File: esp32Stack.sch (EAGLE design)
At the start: 23 parts, among them J02 470, J04 470, J05 470, J12 470, J13 470

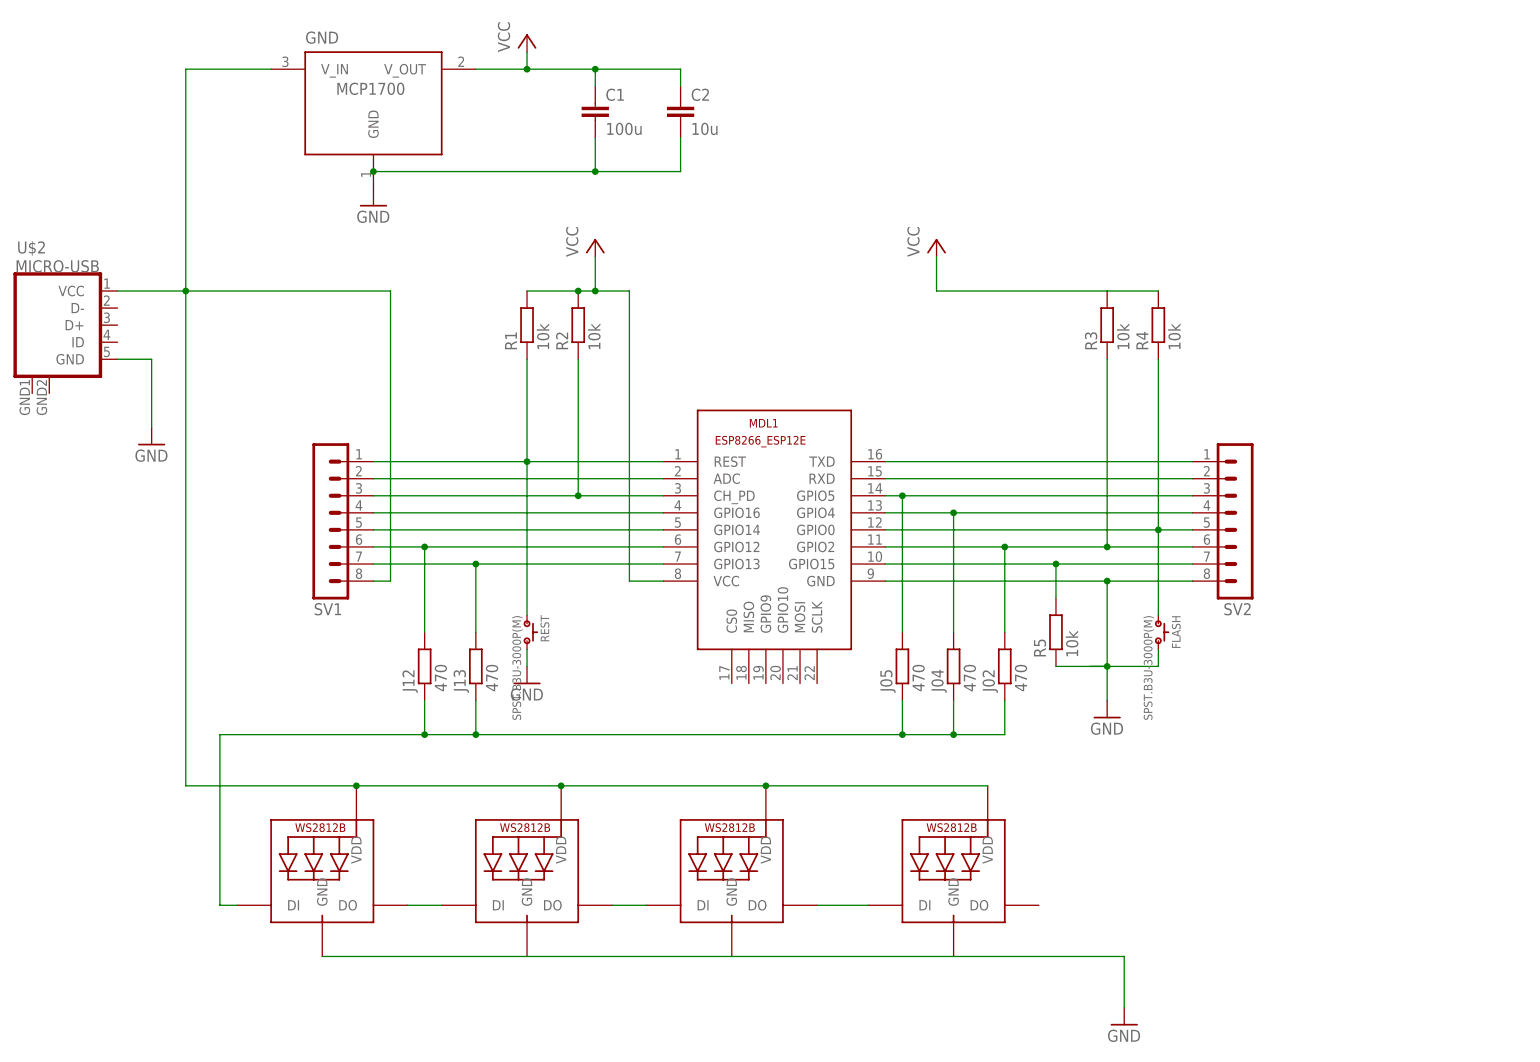
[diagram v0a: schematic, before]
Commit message: added an ftdi version
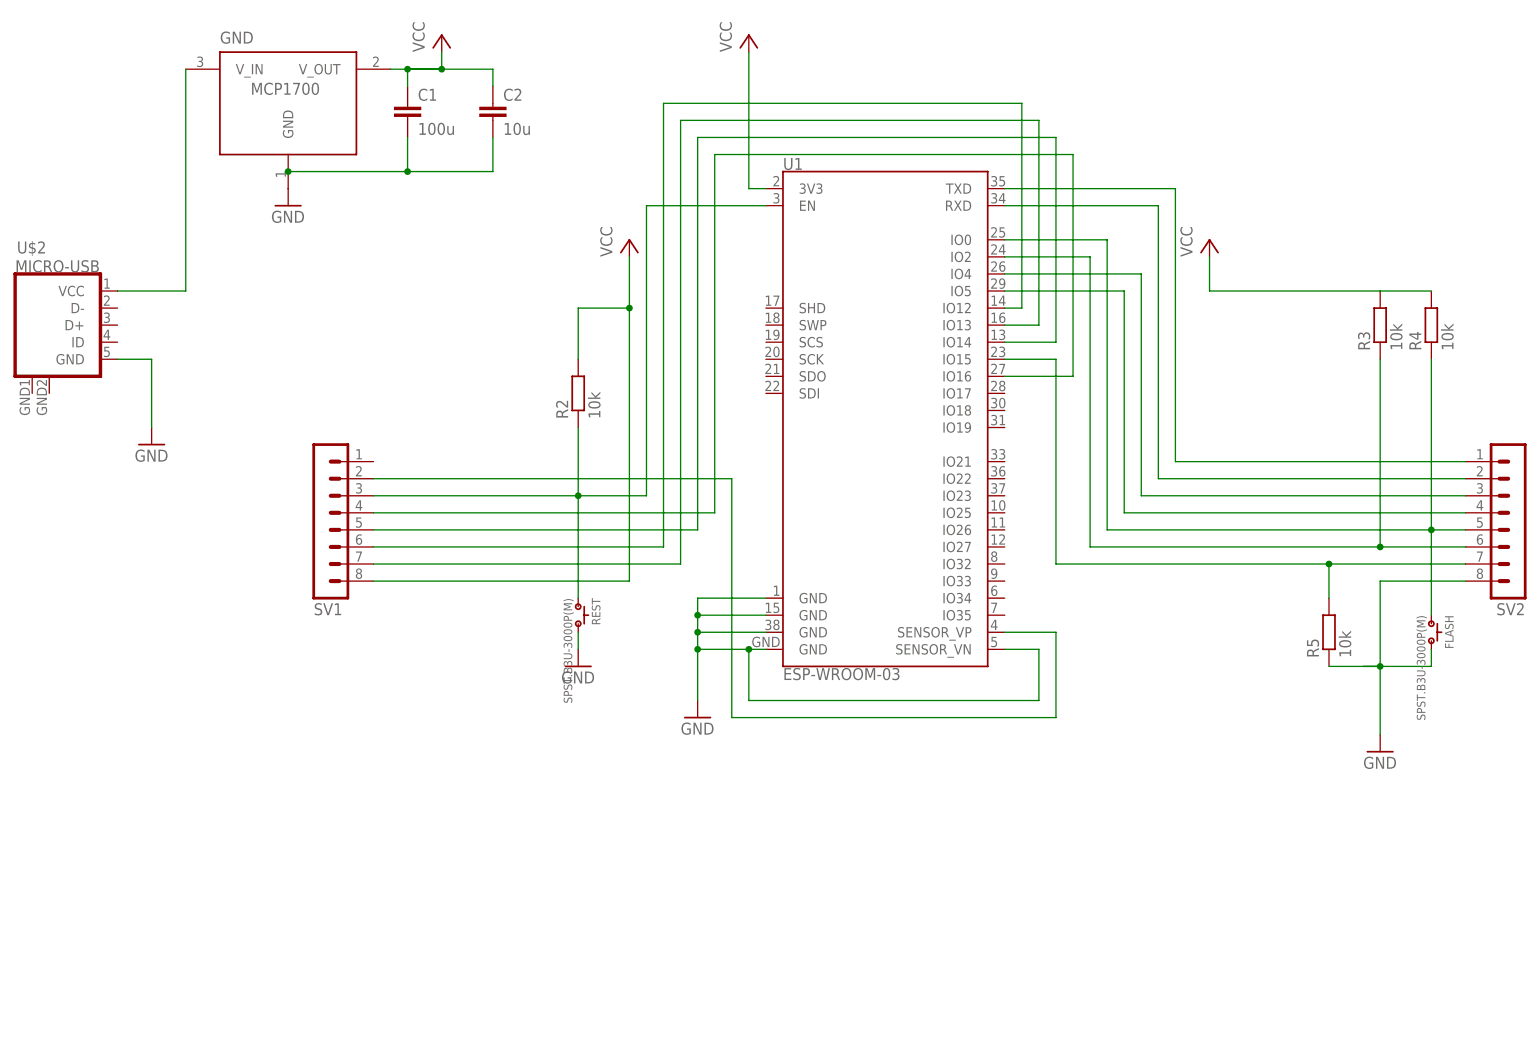
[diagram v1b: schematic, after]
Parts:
- removed J02, J04, J05, J12, J13: 470, eagle-ltspice:R
- removed LED1, LED2, LED3, LED4: WS2812B5050, adafruit:WS2812B5050
- removed MDL1: (no value), ESP12E:ESP8266-12EESP8266-ESP12E
- removed R1: 10k, eagle-ltspice:R
- added U1: ESP-WROOM-03, esp32:ESP-WROOM-03
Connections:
- removed net 3V3: C1.1, C2.1, GND.V_OUT, MDL1.VCC, R1.2, R2.2, R3.2, R4.2
- removed net 5V: GND.V_IN, LED1.VDD, LED2.VDD, LED3.VDD, LED4.VDD, SV1.8, U$2.VCC
- removed net CH_PD: MDL1.CH_PD, R2.1, SV1.3
- removed net DIN: J02.1, J04.1, J05.1, J12.1, J13.1, LED1.DI
- removed net DOUT1DIN2: LED1.DO, LED2.DI
- removed net DOUT2DIN3: LED2.DO, LED3.DI
- removed net DOUT3DIN4: LED3.DO, LED4.DI
- removed net GPIO16: MDL1.GPIO16, SV1.4
- removed net REST: MDL1.REST, R1.1, REST.1, SV1.1
- removed net RXD: MDL1.RXD, SV2.2
- removed net TXD: MDL1.TXD, SV2.1
- new net EN: R2.1, REST.1, SV1.3, U1.EN
- new net N$1: SV2.1, U1.TXD
- new net N$2: SV2.2, U1.RXD
- new net N$3: SV1.5, U1.IO14
- new net N$4: GND.V_IN, U$2.VCC
- new net VCC/V3.3: C1.1, C2.1, GND.V_OUT, R2.2, R3.2, R4.2, SV1.8, U1.3V3
- net ADC: now also U1.SENSOR_VP; no longer MDL1.ADC
- net GND: now also U1.GND, U1.GND@1, U1.GND@15, U1.GND@38, U1.SENSOR_VN; no longer LED1.GND, LED2.GND, LED3.GND, LED4.GND, MDL1.GND
- net GPIO0: now also U1.IO0; no longer MDL1.GPIO0
- net GPIO12: now also U1.IO12; no longer J12.2, MDL1.GPIO12
- net GPIO13: now also U1.IO13; no longer J13.2, MDL1.GPIO13
- net GPIO14: now also SV1.4, U1.IO16; no longer MDL1.GPIO14, SV1.5
- net GPIO15: now also U1.IO15; no longer MDL1.GPIO15
- net GPIO2: now also U1.IO2; no longer J02.2, MDL1.GPIO2
- net GPIO4: now also U1.IO5; no longer J04.2, MDL1.GPIO4
- net GPIO5: now also U1.IO4; no longer J05.2, MDL1.GPIO5
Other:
- moved on the sheet: C1, C2, FLASH, GND, R2, R3, R4, R5, REST, SV2
